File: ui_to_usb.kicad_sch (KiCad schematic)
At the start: 34 parts, among them J1 PM254-2-06-S-8.5, J2 TYPE-C-31-M-12, SW1 RST, SW2 BOOT, U3 USBLC6-2SC6, U5 CH32V203K8T6, U6 SPX3819M5-L, Y2 8M

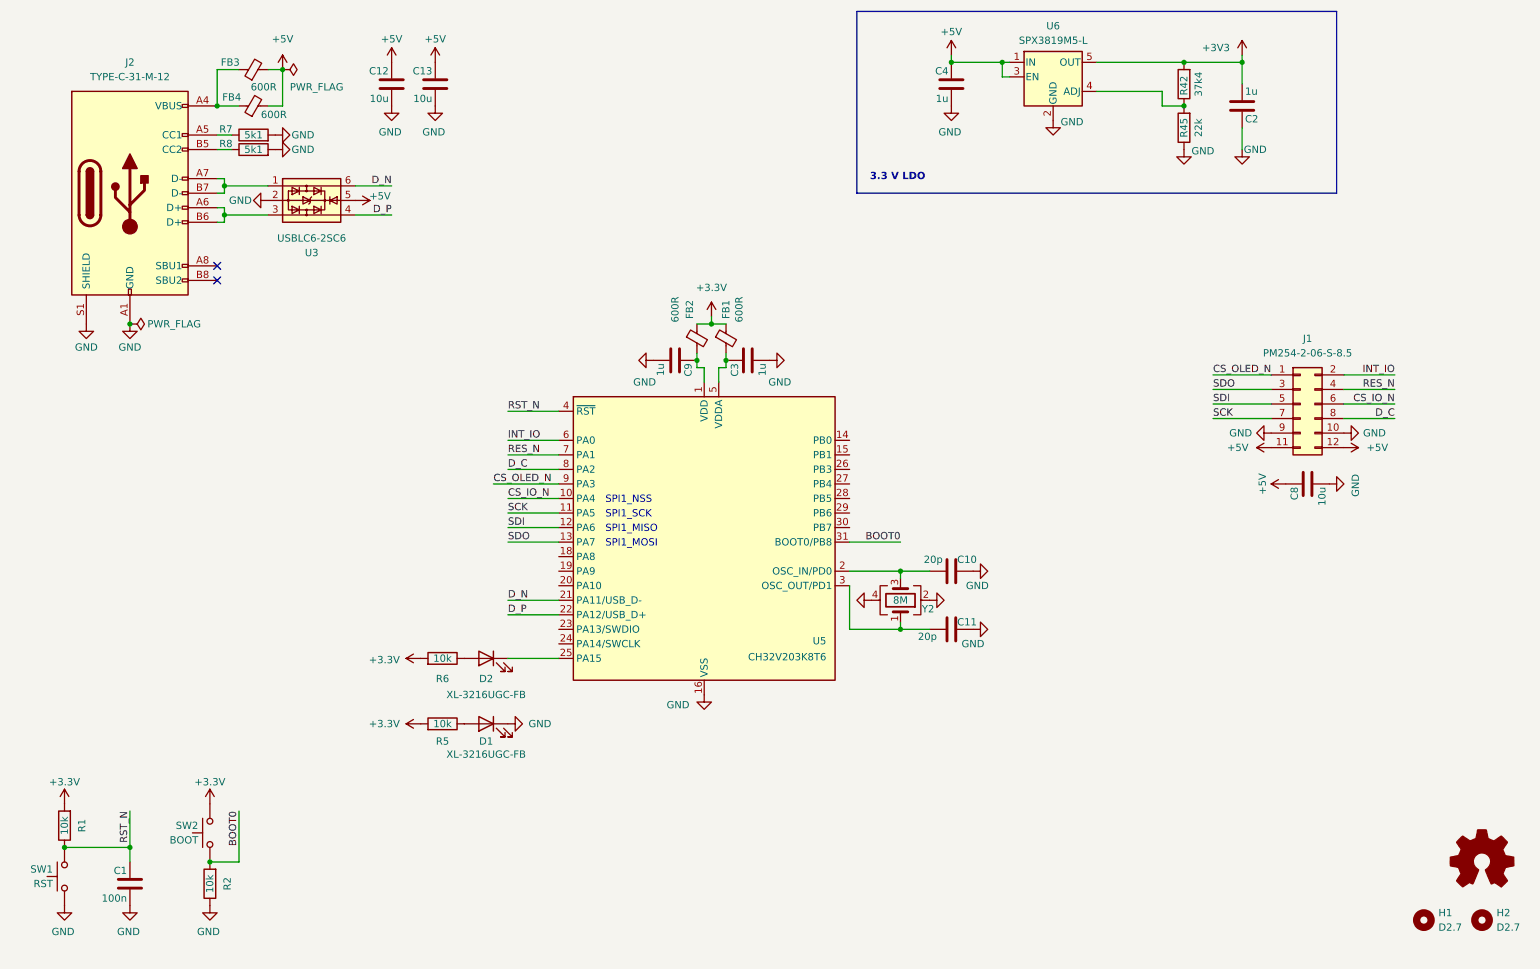
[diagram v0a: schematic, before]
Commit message: add extension port
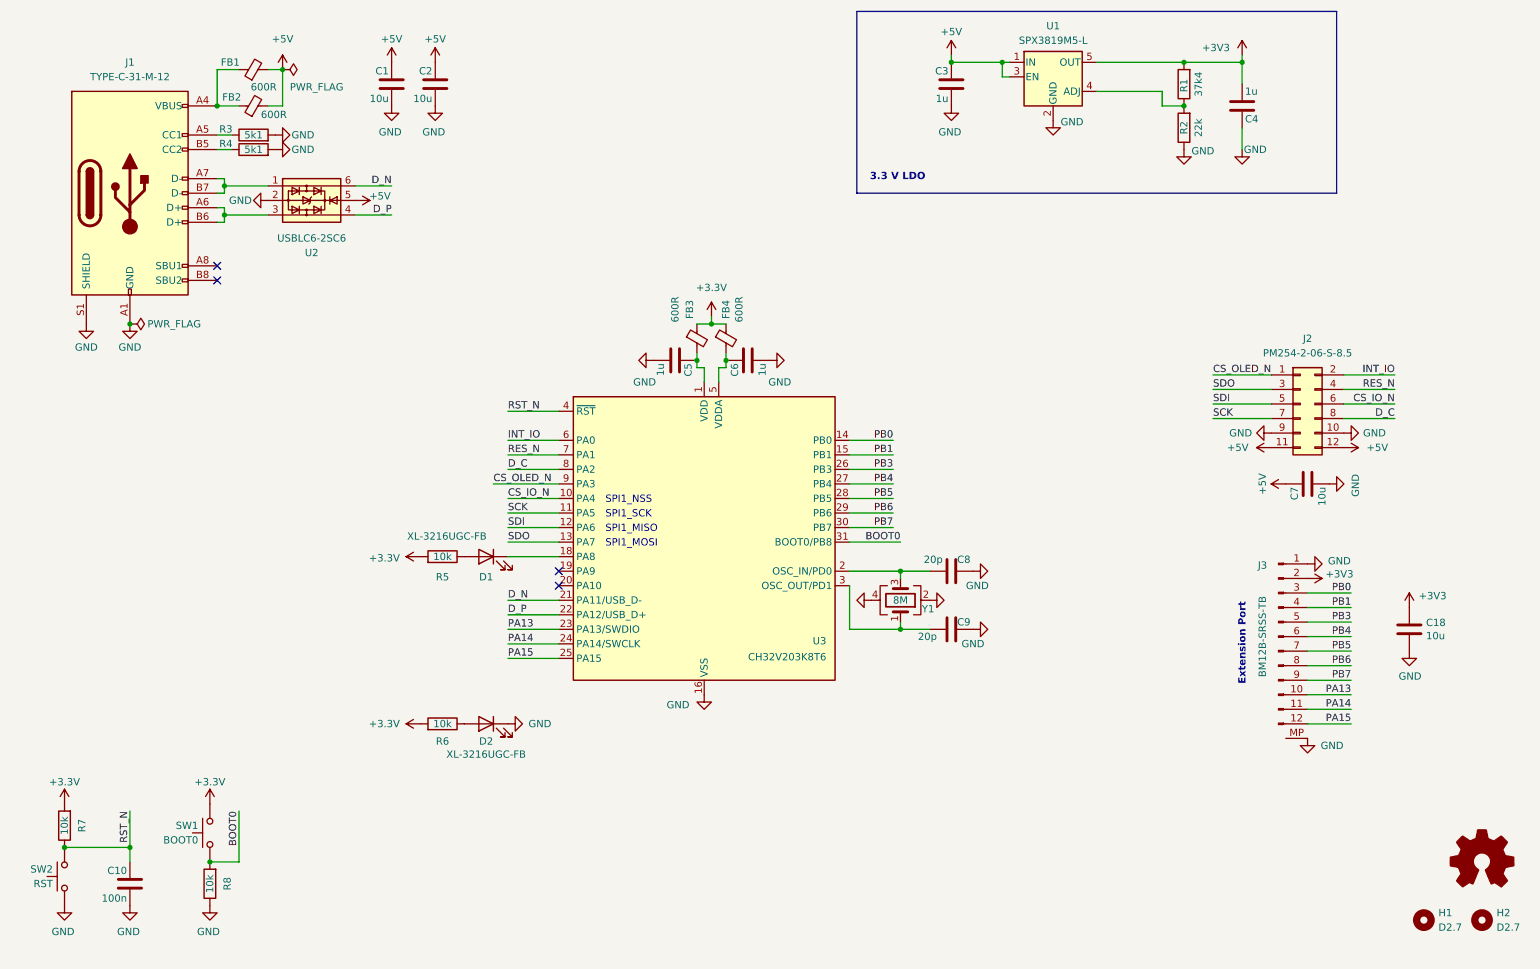
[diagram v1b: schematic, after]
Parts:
- added C18: 10u, Capacitor_SMD:C_1206_3216Metric, symbol Device:C
- added J3: BM12B-SRSS-TB, Connector_JST:JST_SH_BM12B-SRSS-TB_1x12-1MP_P1.00mm_Vertical, symbol Connector:Conn_01x12_Pin
- SW1: renamed from SW2; value BOOT -> BOOT0
- renumbered C12 to C1, C1 to C10, C13 to C2, C4 to C3, C2 to C4, C9 to C5, C3 to C6, C8 to C7, C10 to C8, C11 to C9, D2 to D1, D1 to D2, FB3 to FB1, FB4 to FB2, FB2 to FB3, FB1 to FB4, J2 to J1, J1 to J2, R42 to R1, R45 to R2, R7 to R3, R8 to R4, R6 to R5, R5 to R6, R1 to R7, R2 to R8, SW1 to SW2, U6 to U1, U3 to U2, U5 to U3, Y2 to Y1
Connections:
- net +3V3: now also C18.1, J3.2 (Pin_2)
- net GND: now also C18.2, J3.1 (Pin_1), J3.MP
- net PB0: now reaches U3.14 (PB0)
- net PB0: now also J3.3 (Pin_3)
- net PB1: now reaches U3.15 (PB1)
- net PB1: now also J3.4 (Pin_4)
- net at U3.18 (PA8): now also D1.1 (K)
- net PA13: now reaches U3.23 (PA13/SWDIO)
- net PA13: now also J3.10 (Pin_10)
- net PA14: now reaches U3.24 (PA14/SWCLK)
- net PA14: now also J3.11 (Pin_11)
- net PA15: now reaches U3.25 (PA15)
- net PA15: now also J3.12 (Pin_12); no longer D1.1 (K)
- net PB3: now reaches U3.26 (PB3)
- net PB3: now also J3.5 (Pin_5)
- net PB4: now reaches U3.27 (PB4)
- net PB4: now also J3.6 (Pin_6)
- net PB5: now reaches U3.28 (PB5)
- net PB5: now also J3.7 (Pin_7)
- net PB6: now reaches U3.29 (PB6)
- net PB6: now also J3.8 (Pin_8)
- net PB7: now reaches U3.30 (PB7)
- net PB7: now also J3.9 (Pin_9)
- no-connect marks 2 -> 4
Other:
- note added: "Extension Port"
- moved on the sheet: D1, R5

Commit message: explore placement
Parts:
- added C11: 1u, Capacitor_SMD:C_0603_1608Metric, symbol Device:C
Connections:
- net +3.3V: no longer FB3.1, FB4.1, R7.2, SW1.2
- net +3V3: now also FB3.1, FB4.1, R7.2, SW1.2
- net GND: now also C11.1
- net VDD: now also C11.2
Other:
- moved on the sheet: C5, FB3, FB4

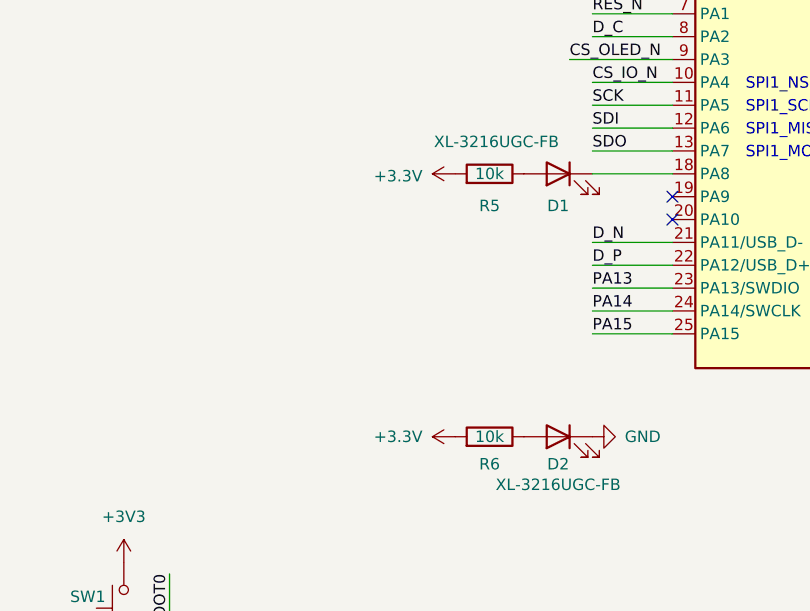
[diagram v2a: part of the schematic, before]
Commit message: switch to 4 layers, all traces routed
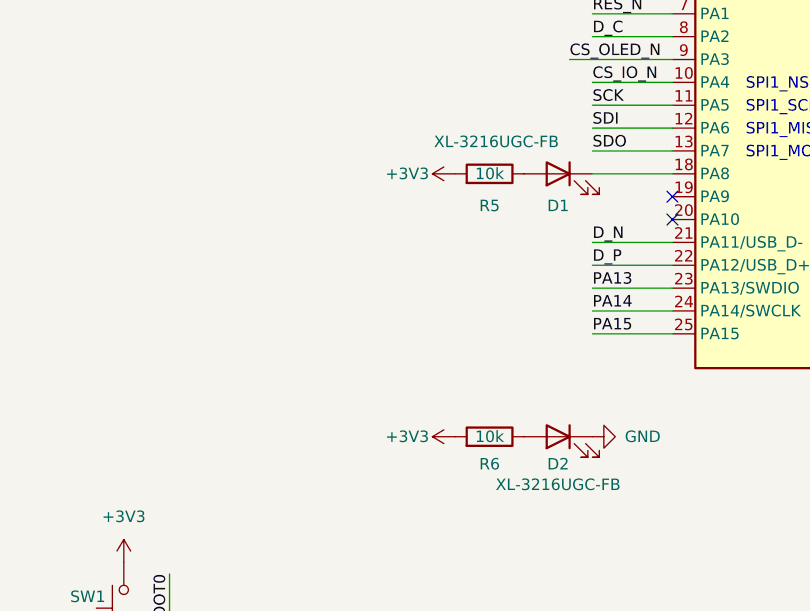
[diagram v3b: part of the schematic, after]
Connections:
- net +3.3V is gone; now on net +3V3: R5.2, R6.2
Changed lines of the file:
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@@
 	)
 	(symbol
-		(lib_id "power:+3.3V")
-		(at 91.44 120.65 90)
-		(mirror x)
-		(unit 1)
-		(exclude_from_sim no)
-		(in_bom yes)
-		(on_board yes)
-		(dnp no)
-		(property "Reference" "#PWR031"
-			(at 95.25 120.65 0)
-			(effects
-				(font
-					(size 1.27 1.27)
-				)
-				(hide yes)
-			)
-		)
-		(property "Value" "+3.3V"
-			(at 85.09 120.904 90)
-			(effects
-				(font
-					(size 1.27 1.27)
-				)
-			)
-		)
-		(property "Footprint" ""
-			(at 91.44 120.65 0)
-			(effects
-				(font
-					(size 1.27 1.27)
-				)
-				(hide yes)
-			)
-		)
-		(property "Datasheet" ""
-			(at 91.44 120.65 0)
-			(effects
-				(font
-					(size 1.27 1.27)
-				)
-				(hide yes)
-			)
-		)
-		(property "Description" "Power symbol creates a global label with name \"+3.3V\""
-			(at 91.44 120.65 0)
-			(effects
-				(font
-					(size 1.27 1.27)
-				)
-				(hide yes)
-			)
-		)
-		(pin "1"
-		)
-		(instances
-			(project "ui_to_usb"
-				(path "/61164785-2abe-4800-8948-e7ba22968736"
-					(reference "#PWR031")
-					(unit 1)
-				)
-			)
-		)
-	)
-	(symbol
 		(lib_id "power:GND")
 		(at 66.04 49.53 90)
@@
 	)
 	(symbol
+		(lib_id "power:+3V3")
+		(at 91.44 120.65 90)
+		(unit 1)
+		(exclude_from_sim no)
+		(in_bom yes)
+		(on_board yes)
+		(dnp no)
+		(property "Reference" "#PWR031"
+			(at 95.25 120.65 0)
+			(effects
+				(font
+					(size 1.27 1.27)
+				)
+				(hide yes)
+			)
+		)
+		(property "Value" "+3V3"
+			(at 86.106 120.65 90)
+			(effects
+				(font
+					(size 1.27 1.27)
+				)
+			)
+		)
+		(property "Footprint" ""
+			(at 91.44 120.65 0)
+			(effects
+				(font
+					(size 1.27 1.27)
+				)
+				(hide yes)
+			)
+		)
+		(property "Datasheet" ""
+			(at 91.44 120.65 0)
+			(effects
+				(font
+					(size 1.27 1.27)
+				)
+				(hide yes)
+			)
+		)
+		(property "Description" ""
+			(at 91.44 120.65 0)
+			(effects
+				(font
+					(size 1.27 1.27)
+				)
+			)
+		)
+		(pin "1"
+		)
+		(instances
+			(project "ui_to_usb"
+				(path "/61164785-2abe-4800-8948-e7ba22968736"
+					(reference "#PWR031")
+					(unit 1)
+				)
+			)
+		)
+	)
+	(symbol
 		(lib_id "power:GND")
 		(at 93.98 41.91 0)
@@
 	)
 	(symbol
-		(lib_id "power:+3.3V")
-		(at 91.44 149.86 90)
-		(mirror x)
-		(unit 1)
-		(exclude_from_sim no)
-		(in_bom yes)
-		(on_board yes)
-		(dnp no)
-		(property "Reference" "#PWR033"
-			(at 95.25 149.86 0)
-			(effects
-				(font
-					(size 1.27 1.27)
-				)
-				(hide yes)
-			)
-		)
-		(property "Value" "+3.3V"
-			(at 85.09 149.86 90)
-			(effects
-				(font
-					(size 1.27 1.27)
-				)
-			)
-		)
-		(property "Footprint" ""
-			(at 91.44 149.86 0)
-			(effects
-				(font
-					(size 1.27 1.27)
-				)
-				(hide yes)
-			)
-		)
-		(property "Datasheet" ""
-			(at 91.44 149.86 0)
-			(effects
-				(font
-					(size 1.27 1.27)
-				)
-				(hide yes)
-			)
-		)
-		(property "Description" "Power symbol creates a global label with name \"+3.3V\""
-			(at 91.44 149.86 0)
-			(effects
-				(font
-					(size 1.27 1.27)
-				)
-				(hide yes)
-			)
-		)
-		(pin "1"
-		)
-		(instances
-			(project "ui_to_usb"
-				(path "/61164785-2abe-4800-8948-e7ba22968736"
-					(reference "#PWR033")
-					(unit 1)
-				)
-			)
-		)
-	)
-	(symbol
 		(lib_id "power:GND")
 		(at 64.77 58.42 270)
@@
 					(unit 1)
 				)
+			)
+		)
+	)
+	(symbol
+		(lib_id "power:+3V3")
+		(at 91.44 149.86 90)
+		(unit 1)
+		(exclude_from_sim no)
+		(in_bom yes)
+		(on_board yes)
+		(dnp no)
+		(property "Reference" "#PWR033"
+			(at 95.25 149.86 0)
+			(effects
+				(font
+					(size 1.27 1.27)
+				)
+				(hide yes)
+			)
+		)
+		(property "Value" "+3V3"
+			(at 86.106 149.86 90)
+			(effects
+				(font
+					(size 1.27 1.27)
+				)
+			)
+		)
+		(property "Footprint" ""
+			(at 91.44 149.86 0)
+			(effects
+				(font
+					(size 1.27 1.27)
+				)
+				(hide yes)
+			)
+		)
+		(property "Datasheet" ""
+			(at 91.44 149.86 0)
+			(effects
+				(font
+					(size 1.27 1.27)
+				)
+				(hide yes)
+			)
+		)
+		(property "Description" ""
+			(at 91.44 149.86 0)
+			(effects
+				(font
+					(size 1.27 1.27)
+				)
+			)
+		)
+		(pin "1"
+		)
+		(instances
+			(project "ui_to_usb"
+				(path "/61164785-2abe-4800-8948-e7ba22968736"
+					(reference "#PWR033")
+					(unit 1)
+				)

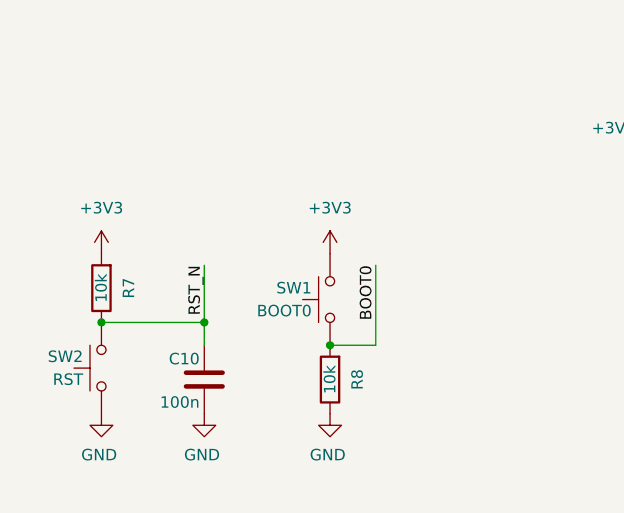
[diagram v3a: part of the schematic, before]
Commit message: add tactile button footprint
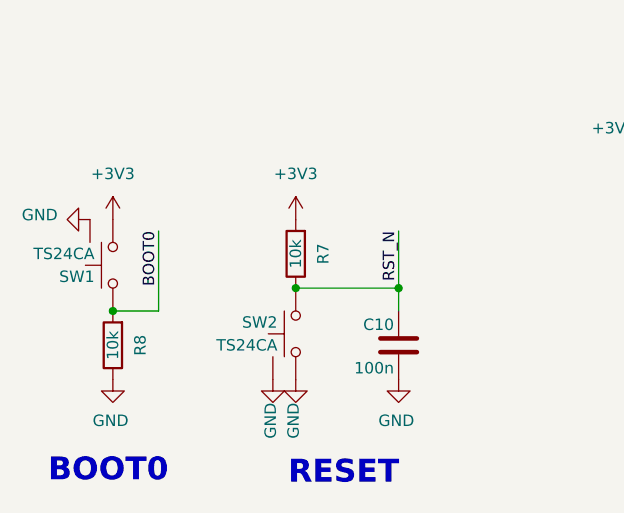
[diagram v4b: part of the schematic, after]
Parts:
- SW1: value BOOT0 -> TS24CA; footprint Button_Switch_SMD:SW_SPST_B3U-3000P-B -> footprints:TS24CA
- SW2: value RST -> TS24CA; footprint Button_Switch_SMD:SW_SPST_B3U-3000P-B -> footprints:TS24CA
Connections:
- net +3V3: now also SW1.1; no longer SW1.2
- net BOOT0: now also SW1.2; no longer SW1.1
- net GND: now also SW1.0, SW2.0
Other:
- note added: "BOOT0"
- note added: "RESET"
- moved on the sheet: C10, R7, R8

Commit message: Layout looks decent. Ready to order.
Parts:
- added TP1: U_TX, TestPoint:TestPoint_Pad_D1.0mm, symbol Connector:TestPoint_Small
- added TP2: U_RX, TestPoint:TestPoint_Pad_D1.0mm, symbol Connector:TestPoint_Small
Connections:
- net at U3.19 (PA9): now also TP1.1
- net at U3.20 (PA10): now also TP2.1
- no-connect marks 4 -> 2
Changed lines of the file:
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@@
 	(title_block
 		(title "ui_to_usb")
-		(date "2025-12-28")
-		(rev "-")
+		(date "2026-02-12")
+		(rev "1")
 		(company "Betz Engineering")
 		(comment 1 "USB adapter for ui_board_1u")
@@
 	)
 	(no_connect
-		(at 115.57 123.19)
-	)
-	(no_connect
-		(at 115.57 125.73)
-	)
-	(no_connect
 		(at 55.88 69.85)
 	)
@@
 	(wire
 		(pts
+			(xy 114.3 125.73) (xy 115.57 125.73)
+		)
+		(stroke
+			(width 0)
+			(type default)
+		)
+	)
+	(wire
+		(pts
 			(xy 106.68 135.89) (xy 115.57 135.89)
 		)
@@
 	(wire
 		(pts
+			(xy 114.3 123.19) (xy 115.57 123.19)
+		)
+		(stroke
+			(width 0)
+			(type default)
+		)
+	)
+	(wire
+		(pts
 			(xy 55.88 57.15) (xy 57.15 57.15)
 		)
@@
 	)
 	(symbol
+		(lib_id "Connector:TestPoint_Small")
+		(at 114.3 123.19 0)
+		(unit 1)
+		(exclude_from_sim no)
+		(in_bom yes)
+		(on_board yes)
+		(dnp no)
+		(property "Reference" "TP1"
+			(at 113.03 121.9199 0)
+			(effects
+				(font
+					(size 1.27 1.27)
+				)
+				(justify right)
+			)
+		)
+		(property "Value" "U_TX"
+			(at 119.888 125.476 0)
+			(effects
+				(font
+					(size 1.27 1.27)
+				)
+				(justify right)
+				(hide yes)
+			)
+		)
+		(property "Footprint" "TestPoint:TestPoint_Pad_D1.0mm"
+			(at 119.38 123.19 0)
+			(effects
+				(font
+					(size 1.27 1.27)
+				)
+				(hide yes)
+			)
+		)
+		(property "Datasheet" "~"
+			(at 119.38 123.19 0)
+			(effects
+				(font
+					(size 1.27 1.27)
+				)
+				(hide yes)
+			)
+		)
+		(property "Description" "test point"
+			(at 114.3 123.19 0)
+			(effects
+				(font
+					(size 1.27 1.27)
+				)
+				(hide yes)
+			)
+		)
+		(pin "1"
+		)
+		(instances
+			(project ""
+				(path "/61164785-2abe-4800-8948-e7ba22968736"
+					(reference "TP1")
+					(unit 1)
+				)
+			)
+		)
+	)
+	(symbol
 		(lib_id "power:GND")
 		(at 66.04 46.99 90)
@@
 					(unit 1)
 				)
+			)
+		)
+	)
+	(symbol
+		(lib_id "Connector:TestPoint_Small")
+		(at 114.3 125.73 0)
+		(unit 1)
+		(exclude_from_sim no)
+		(in_bom yes)
+		(on_board yes)
+		(dnp no)
+		(property "Reference" "TP2"
+			(at 113.03 124.4599 0)
+			(effects
+				(font
+					(size 1.27 1.27)
+				)
+				(justify right)
+			)
+		)
+		(property "Value" "U_RX"
+			(at 119.888 128.016 0)
+			(effects
+				(font
+					(size 1.27 1.27)
+				)
+				(justify right)
+				(hide yes)
+			)
+		)
+		(property "Footprint" "TestPoint:TestPoint_Pad_D1.0mm"
+			(at 119.38 125.73 0)
+			(effects
+				(font
+					(size 1.27 1.27)
+				)
+				(hide yes)
+			)
+		)
+		(property "Datasheet" "~"
+			(at 119.38 125.73 0)
+			(effects
+				(font
+					(size 1.27 1.27)
+				)
+				(hide yes)
+			)
+		)
+		(property "Description" "test point"
+			(at 114.3 125.73 0)
+			(effects
+				(font
+					(size 1.27 1.27)
+				)
+				(hide yes)
+			)
+		)
+		(pin "1"
+		)
+		(instances
+			(project "ui_to_usb"
+				(path "/61164785-2abe-4800-8948-e7ba22968736"
+					(reference "TP2")
+					(unit 1)
+				)
